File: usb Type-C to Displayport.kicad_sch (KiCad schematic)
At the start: 22 parts, among them CN1 HYC16-DP20-178, J1 USB_C_Receptacle, U1 VL103-Q3, U2 W25Q16BVSSIG

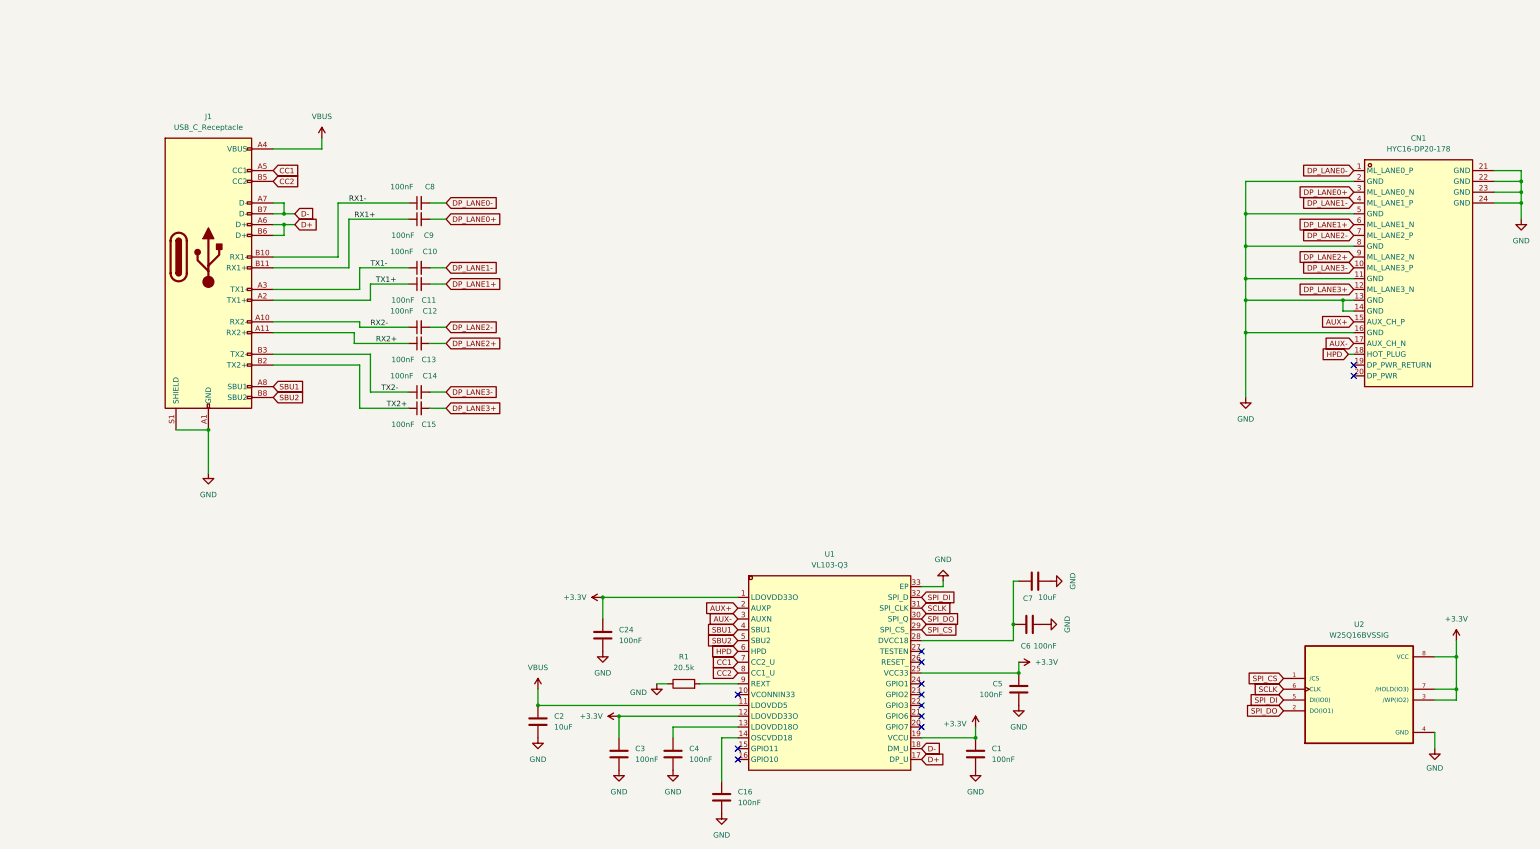
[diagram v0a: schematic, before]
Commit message: 0.2
Removed SPI chip, fixed CC lines being reversed, made pcb smaller, added mounting holes
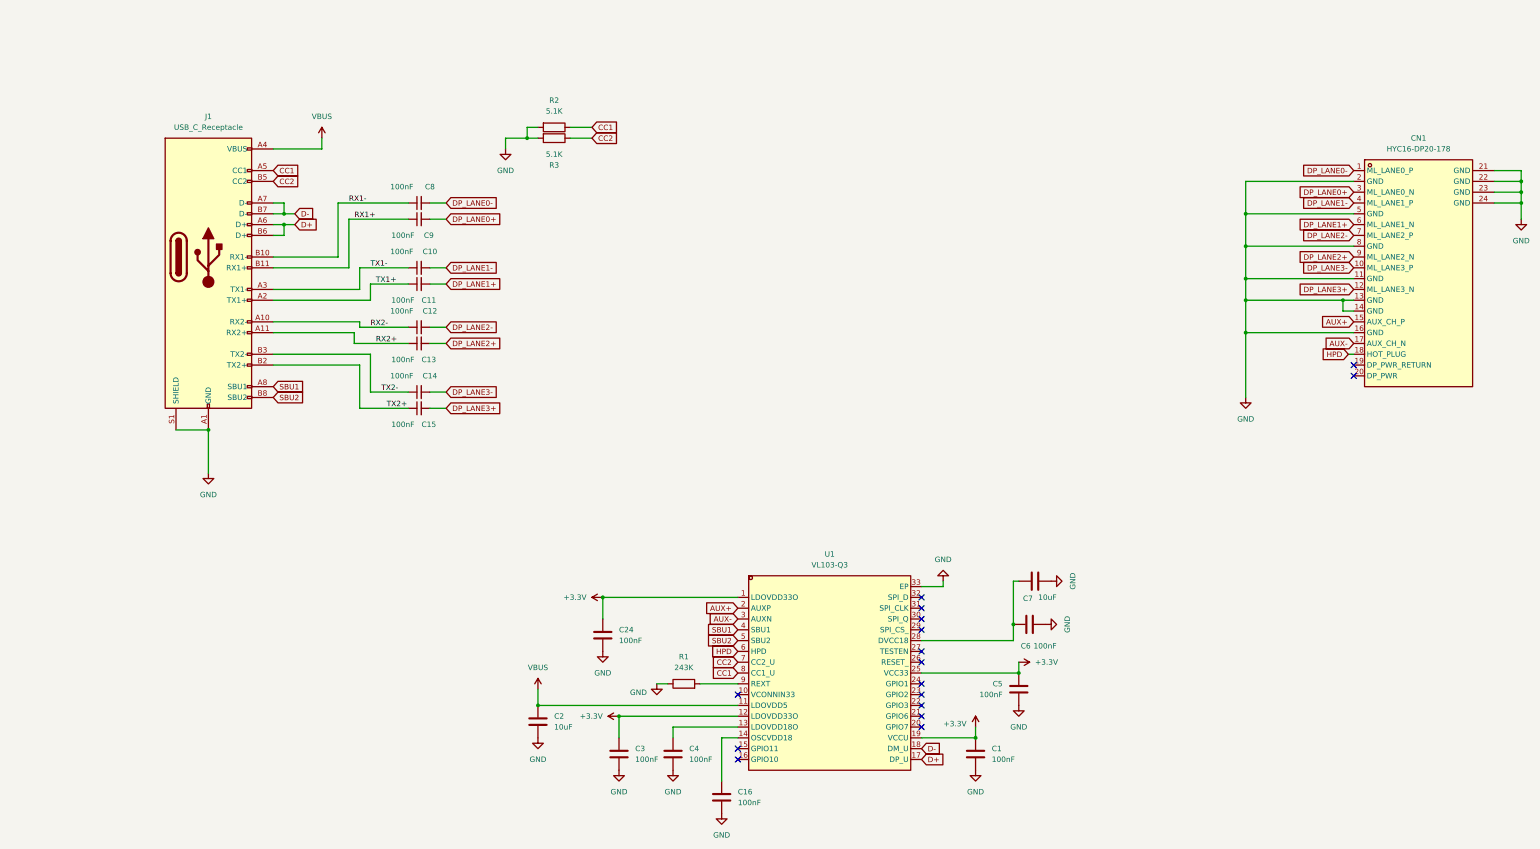
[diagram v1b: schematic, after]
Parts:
- removed U2: W25Q16BVSSIG, da:SOIC-8_L5.0-W4.0-P1.27-LS6.0-BL, symbol W25Q16BV:W25Q16BVSSIG
- added R2, R3: 5.1K, Resistor_SMD:R_0402_1005Metric, symbol Device:R
- R1: value 20.5k -> 243K
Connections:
- net CC1: now also U1.8 (CC1_U), R2.1; no longer U1.7 (CC2_U)
- net CC2: now also U1.7 (CC2_U), R3.1; no longer U1.8 (CC1_U)
- net GND: now also R2.2, R3.2
- net SCLK: no longer names the net of U1.31 (SPI_CLK)
- net SPI_CS: no longer names the net of U1.29 (SPI_CS_)
- net SPI_DI: no longer names the net of U1.32 (SPI_D)
- net SPI_DO: no longer names the net of U1.30 (SPI_Q)
- no-connect marks 12 -> 16

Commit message: Changed IC to vl100 q3
Changed ic to vl100 q3 (i found it cheaper and it's pin compatible, added Crystal)
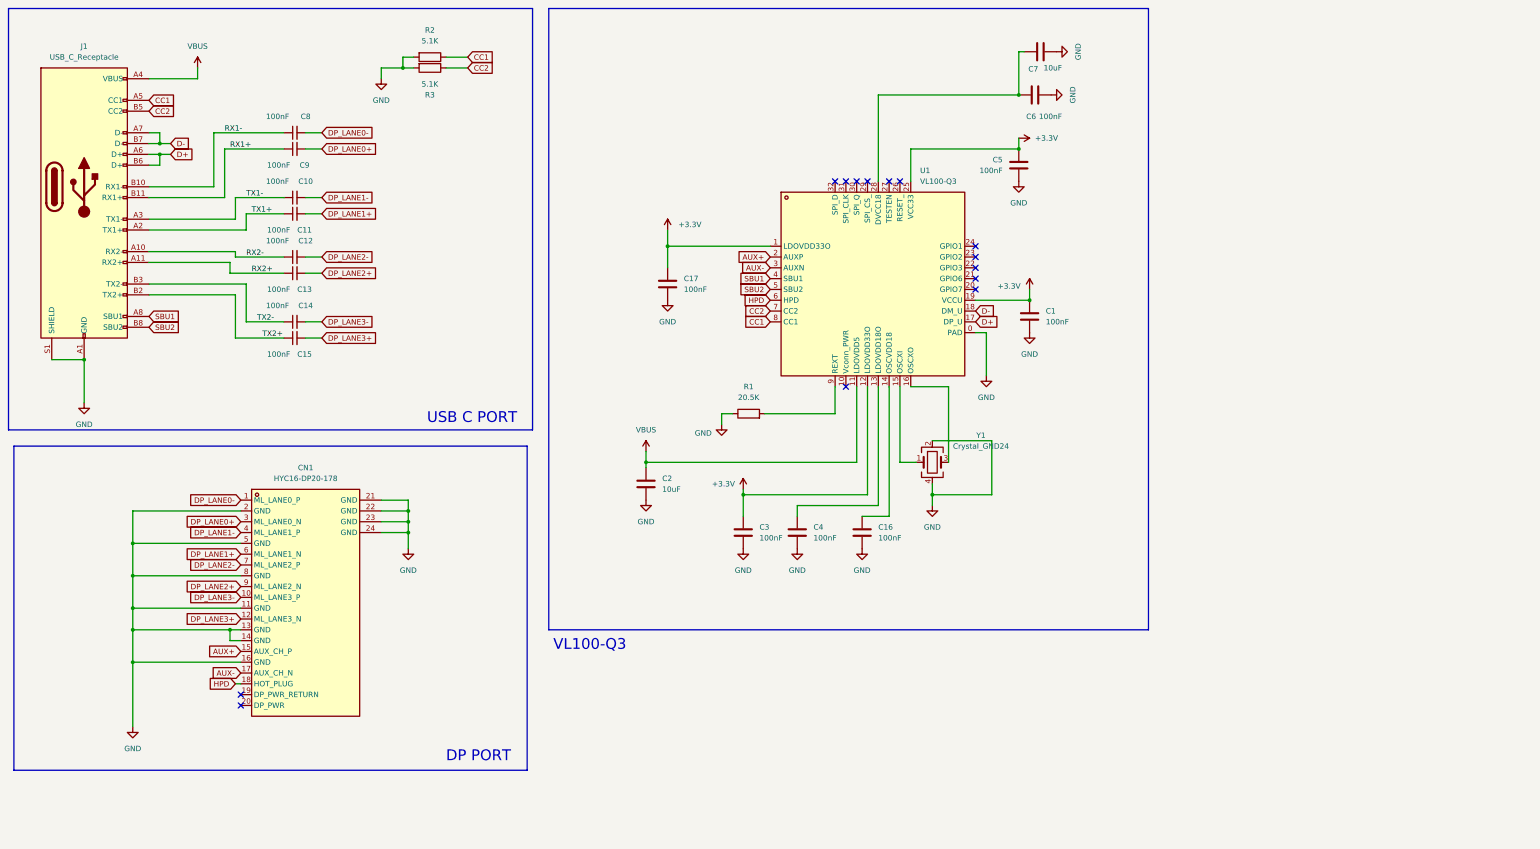
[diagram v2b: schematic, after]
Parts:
- removed C24: 100nF, Capacitor_SMD:C_0402_1005Metric_Pad0.74x0.62mm_HandSolder, symbol Device:C
- removed U1: VL103-Q3, da:QFN-32_L5.0-W5.0-P0.50-TL-EP3.5, symbol da:VL103-Q3
- added C17: 100nF, Capacitor_SMD:C_0402_1005Metric_Pad0.74x0.62mm_HandSolder, symbol Device:C
- added U1: VL100-Q3, da:QFN-32_L5.0-W5.0-P0.50-BL-EP3.4, symbol da:VL100-Q3
- added Y1: Crystal_GND24, Crystal:Crystal_SMD_3225-4Pin_3.2x2.5mm, symbol Device:Crystal_GND24
- R1: value 243K -> 20.5K
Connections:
- net +3.3V: now also C17.1, U1.1 (LDOVDD33O), U1.12 (LDOVDD33O), U1.19 (VCCU), U1.25 (VCC33)
- net AUX+: now also U1.2 (AUXP)
- net AUX-: now also U1.3 (AUXN)
- net CC1: now also U1.8 (CC1)
- net CC2: now also U1.7 (CC2)
- net D+: now also U1.17 (DP_U)
- net D-: now also U1.18 (DM_U)
- net GND: now also C17.2, U1.0 (PAD), Y1.2, Y1.4
- net HPD: now also U1.6 (HPD)
- net SBU1: now also U1.4 (SBU1)
- net SBU2: now also U1.5 (SBU2)
- net VBUS: now also U1.11 (LDOVDD5)
- net at C6.1, C7.1: now also U1.28 (DVCC18)
- net at C16.1: now also U1.14 (OSCVDD18)
- net at C4.1: now also U1.13 (LDOVDD18O)
- net at R1.2: now also U1.9 (REXT)
- new net: U1.15 (OSCXI), Y1.1
- new net: U1.16 (OSCXO), Y1.3
- no-connect marks 16 -> 14
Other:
- note added: "DP PORT"
- note added: "USB C PORT"
- note added: "VL100-Q3"
- moved on the sheet: C10, C11, C12, C13, C14, C15, C8, C9, CN1, J1, R2, R3

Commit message: Fixed usb footprint
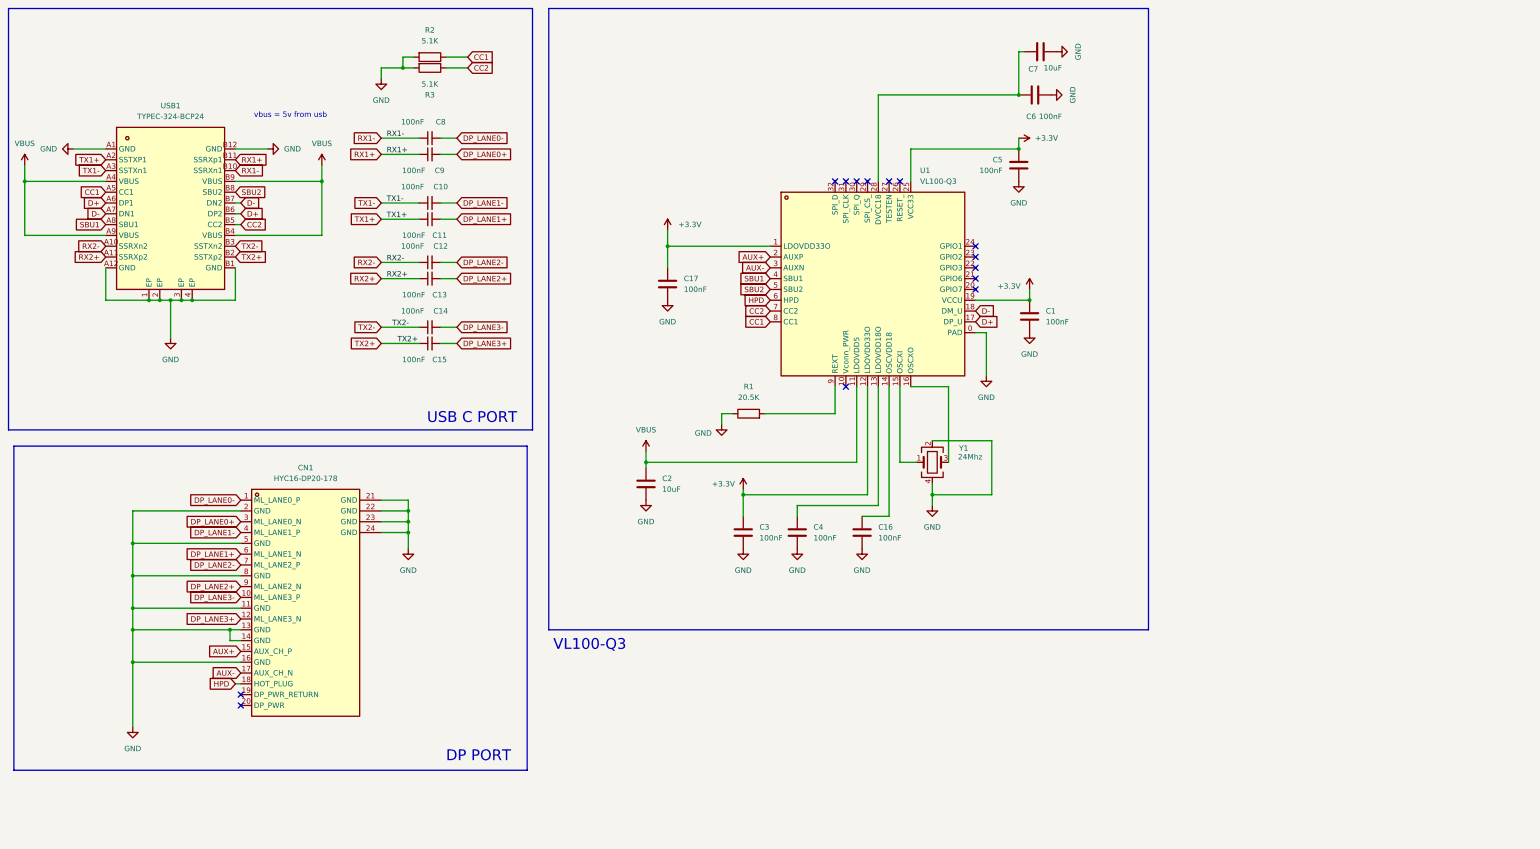
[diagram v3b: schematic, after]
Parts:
- removed J1: USB_C_Receptacle, Connector_USB:USB_C_Receptacle_Amphenol_12401548E4-2A, symbol Connector:USB_C_Receptacle
- added USB1: TYPEC-324-BCP24, da:USB-C-SMD_TYPEC-324-BCP24, symbol da:TYPEC-324-BCP24
- Y1: value Crystal_GND24 -> 24Mhz
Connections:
- net CC1: now also USB1.A5 (CC1)
- net CC2: now also USB1.B5 (CC2)
- net D+: now also USB1.A6 (DP1), USB1.B6 (DP2)
- net D-: now also USB1.A7 (DN1), USB1.B7 (DN2)
- net GND: now also USB1.1 (EP), USB1.2 (EP), USB1.3 (EP), USB1.4 (EP), USB1.A1 (GND), USB1.A12 (GND), USB1.B1 (GND), USB1.B12 (GND)
- net RX1+: now also USB1.B11 (SSRXp1)
- net RX1-: now also USB1.B10 (SSRXn1)
- net RX2+: now also USB1.A11 (SSRXp2)
- net RX2-: now also USB1.A10 (SSRXn2)
- net SBU1: now also USB1.A8 (SBU1)
- net SBU2: now also USB1.B8 (SBU2)
- net TX1+: now also USB1.A2 (SSTXP1)
- net TX1-: now also USB1.A3 (SSTXn1)
- net TX2+: now also USB1.B2 (SSTXp2)
- net TX2-: now also USB1.B3 (SSTXn2)
- net VBUS: now also USB1.A4 (VBUS), USB1.A9 (VBUS), USB1.B4 (VBUS), USB1.B9 (VBUS)
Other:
- note added: "vbus = 5v from usb"
- moved on the sheet: C10, C11, C12, C13, C14, C15, C8, C9

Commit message: Fixed DP lines
Fixed wrong USB lines to DP lines, fixed differential pairs not length matched, length matched all 4 pairs
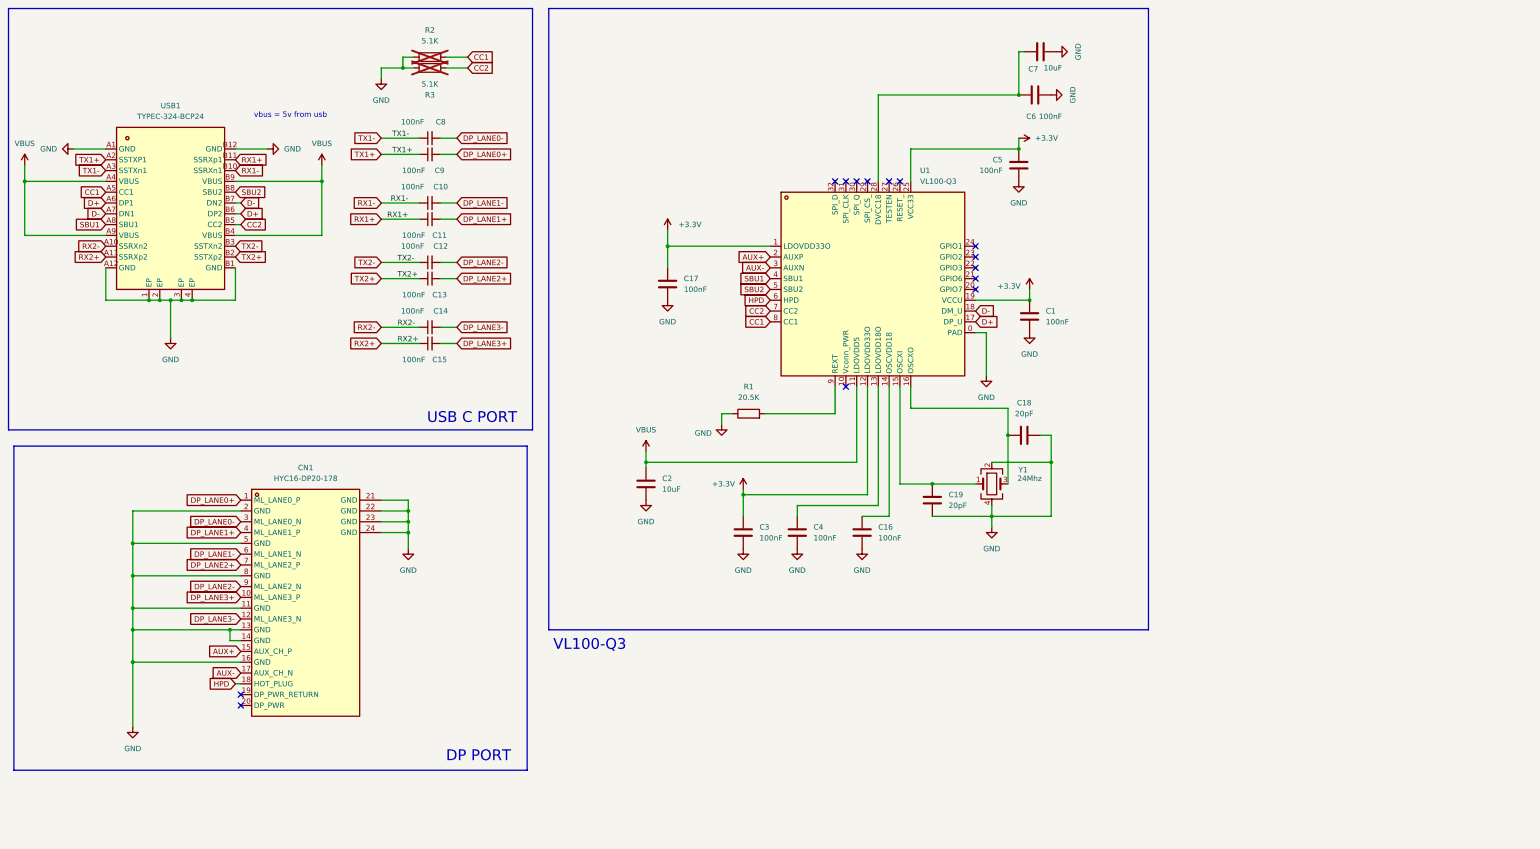
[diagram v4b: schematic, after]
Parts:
- added C18, C19: 20pF, Capacitor_SMD:C_0402_1005Metric, symbol Device:C
- R2, R3: now not fitted
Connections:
- net DP_LANE0+: now also CN1.1 (ML_LANE0_P); no longer CN1.3 (ML_LANE0_N)
- net DP_LANE0-: now also CN1.3 (ML_LANE0_N); no longer CN1.1 (ML_LANE0_P)
- net DP_LANE1+: now also CN1.4 (ML_LANE1_P); no longer CN1.6 (ML_LANE1_N)
- net DP_LANE1-: now also CN1.6 (ML_LANE1_N); no longer CN1.4 (ML_LANE1_P)
- net DP_LANE2+: now also CN1.7 (ML_LANE2_P); no longer CN1.9 (ML_LANE2_N)
- net DP_LANE2-: now also CN1.9 (ML_LANE2_N); no longer CN1.7 (ML_LANE2_P)
- net DP_LANE3+: now also CN1.10 (ML_LANE3_P); no longer CN1.12 (ML_LANE3_N)
- net DP_LANE3-: now also CN1.12 (ML_LANE3_N); no longer CN1.10 (ML_LANE3_P)
- net GND: now also C18.2, C19.1
- net RX1+: now also C11.1; no longer C9.1
- net RX1-: now also C10.1; no longer C8.1
- net RX2+: now also C15.1; no longer C13.1
- net RX2-: now also C14.1; no longer C12.1
- net TX1+: now also C9.1; no longer C11.1
- net TX1-: now also C8.1; no longer C10.1
- net TX2+: now also C13.1; no longer C15.1
- net TX2-: now also C12.1; no longer C14.1
- net at U1.15 (OSCXI), Y1.1: now also C19.2
- net at U1.16 (OSCXO), Y1.3: now also C18.1
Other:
- moved on the sheet: Y1
